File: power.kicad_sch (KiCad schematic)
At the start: 116 parts, among them J3 Conn_01x01, J4 Conn_01x01, U16 CSD95472Q5MC, U3 TPS53647, U36 MCP1824T-1802E, U4 CSD95472Q5MC, U5 CSD95472Q5MC, U6 AP3211, U7 MCP1824T-0802E

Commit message: Added 4th Phase Buck
Started to add 4th Phase for the Buck, implementing BM1370 footprint etc
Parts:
- added C198: 100n/0.7mm, Capacitor_SMD:C_0805_2012Metric, symbol Device:C
- added C199: 2.2µ, Capacitor_SMD:C_0805_2012Metric, symbol Device:C
- added C200: 100n, Capacitor_SMD:C_0805_2012Metric, symbol Device:C
- added C201, C202: 1n/0.7mm, Capacitor_SMD:C_0805_2012Metric, symbol Device:C
- added C206, C207: 100µ/6.3V, Capacitor_SMD:C_1210_3225Metric, symbol Device:C
- added C208, C209, C210, C214: 330µ/4V, Capacitor_SMD:C_1210_3225Metric, symbol Device:C
- added C215: 3.3n/25V, Capacitor_SMD:C_0805_2012Metric, symbol Device:C
- added C216: 1µ/25V, Capacitor_SMD:C_0805_2012Metric, symbol Device:C
- added C217: 10µ, Capacitor_SMD:C_0805_2012Metric, symbol Device:C
- added C218: 220µ/25V, Capacitor_SMD:CP_Elec_8x10, symbol Device:C_Polarized
- added C222, C223, C224: 22µ/25V, Capacitor_SMD:C_1210_3225Metric, symbol Device:C
- added L5: 220nH, Qaxe:IFLR-4031GC-01-8x10, symbol Device:L
- added R52, R53: 1R/0.5W, Resistor_SMD:R_0805_2012Metric, symbol Device:R
- added U1: CSD95472Q5MC, myfootprints:CSD95472-SON-5x6, symbol mylib7:CSD95472Q5MC
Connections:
- net +12V: now also C215.1, C216.1, C218.1, C222.1, C223.1, C224.1, U1.7 (VIN)
- net +1V2: now also C206.1, C207.1, C208.1, C209.1, C210.1, C214.1, L5.2
- net +3V3: no longer U3.6 (CSP4)
- net +5V: now also C217.1, R52.1
- net +VRef: now also C198.1, U1.2 (REFIN)
- net FCCM: now also U1.10 (FCCM)
- net GND: now also C198.2, C199.2, C201.2, C202.2, C206.2, C207.2, C208.2, C209.2, C210.2, C214.2, C215.2, C216.2, C217.2, C218.2, C222.2, C223.2, C224.2, U1.13 (PGND), U1.4 (PGND)
- net TPS_TSEN: now also C202.1, U1.11 (TAO/FAULT)
- net TPS_PWM4: now reaches U3.35 (PWM4)
- net TPS_PWM4: now also U1.12 (PWM)
- new net: C201.1, R53.1
- new net: L5.1, R53.2, U1.6 (VSW)
- new net: C199.1, R52.2, U1.3 (ENABLE), U1.5 (VDD)
- new net: C200.2, U1.8 (BOOT_R)
- new net: C200.1, U1.9 (BOOT)
- new net TPS_CSP4: U1.1 (IOUT), U3.6 (CSP4)
- no-connect marks 11 -> 10
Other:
- moved on the sheet: C1, C10, C100, C104, C106, C109, C11, C110, C112, C113, C117, C118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

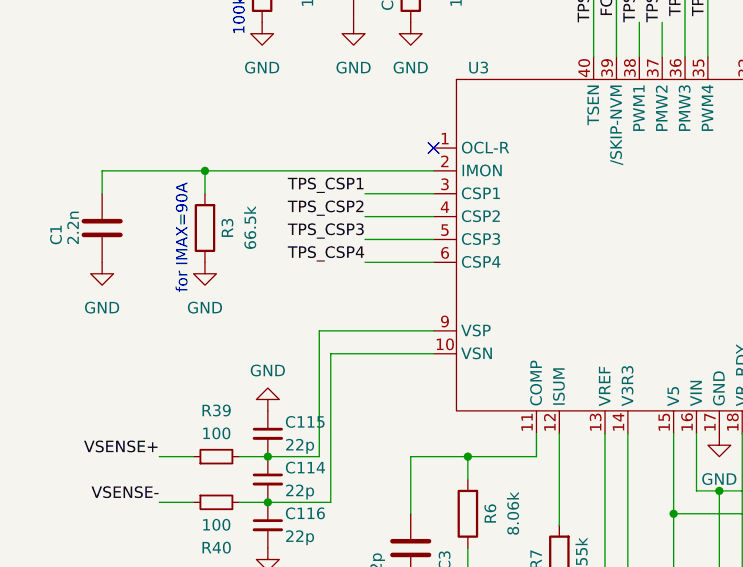
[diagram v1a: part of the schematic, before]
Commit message: Phase4 Disable
Phase4-Disable Jumper
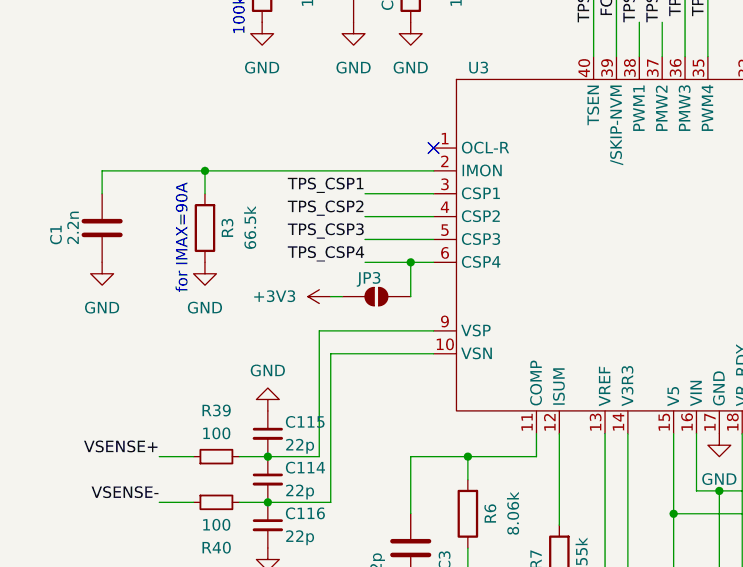
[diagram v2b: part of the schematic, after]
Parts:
- added JP3: Disable Phase 4, Jumper:SolderJumper-2_P1.3mm_Open_RoundedPad1.0x1.5mm, symbol Jumper:SolderJumper_2_Open
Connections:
- net +3V3: now also JP3.1 (A)
- net TPS_CSP4: now also JP3.2 (B)
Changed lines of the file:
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@@
 	)
 	(junction
+		(at 62.23 123.19)
+		(diameter 0)
+		(color 0 0 0 0)
+	)
+	(junction
 		(at 354.33 120.65)
 		(diameter 0)
@@
 	(wire
 		(pts
+			(xy 53.34 127) (xy 54.61 127)
+		)
+		(stroke
+			(width 0)
+			(type default)
+		)
+	)
+	(wire
+		(pts
 			(xy 190.5 50.8) (xy 195.58 50.8)
 		)
@@
 	(wire
 		(pts
-			(xy 57.15 123.19) (xy 64.77 123.19)
+			(xy 57.15 123.19) (xy 62.23 123.19)
 		)
 		(stroke
@@
 	(wire
 		(pts
+			(xy 62.23 127) (xy 62.23 123.19)
+		)
+		(stroke
+			(width 0)
+			(type default)
+		)
+	)
+	(wire
+		(pts
 			(xy 43.18 149.86) (xy 46.355 149.86)
 		)
@@
 	(wire
 		(pts
+			(xy 62.23 123.19) (xy 64.77 123.19)
+		)
+		(stroke
+			(width 0)
+			(type default)
+		)
+	)
+	(wire
+		(pts
 			(xy 311.15 116.84) (xy 311.15 120.65)
 		)
@@
 	)
 	(symbol
+		(lib_id "Jumper:SolderJumper_2_Open")
+		(at 58.42 127 0)
+		(unit 1)
+		(exclude_from_sim yes)
+		(in_bom no)
+		(on_board yes)
+		(dnp no)
+		(property "Reference" "JP3"
+			(at 57.658 124.968 0)
+			(effects
+				(font
+					(size 1.27 1.27)
+				)
+			)
+		)
+		(property "Value" "Disable Phase 4"
+			(at 55.372 129.032 0)
+			(effects
+				(font
+					(size 1.27 1.27)
+				)
+				(hide yes)
+			)
+		)
+		(property "Footprint" "Jumper:SolderJumper-2_P1.3mm_Open_RoundedPad1.0x1.5mm"
+			(at 58.42 127 0)
+			(effects
+				(font
+					(size 1.27 1.27)
+				)
+				(hide yes)
+			)
+		)
+		(property "Datasheet" "~"
+			(at 58.42 127 0)
+			(effects
+				(font
+					(size 1.27 1.27)
+				)
+				(hide yes)
+			)
+		)
+		(property "Description" "Solder Jumper, 2-pole, open"
+			(at 58.42 127 0)
+			(effects
+				(font
+					(size 1.27 1.27)
+				)
+				(hide yes)
+			)
+		)
+		(pin "2"
+		)
+		(pin "1"
+		)
+		(instances
+			(project "Nerd8"
+				(path "/e63e39d7-6ac0-4ffd-8aa3-1841a4541b55/8ec0a9c6-2b78-44ef-a83d-9047d2828409"
+					(reference "JP3")
+					(unit 1)
+				)
+			)
+		)
+	)
+	(symbol
 		(lib_id "Device:C")
 		(at 195.58 68.58 0)
@@
 					(unit 1)
 				)
+			)
+		)
+	)
+	(symbol
+		(lib_name "+3V3_2")
+		(lib_id "power:+3V3")
+		(at 53.34 127 90)
+		(unit 1)
+		(exclude_from_sim no)
+		(in_bom yes)
+		(on_board yes)
+		(dnp no)
+		(fields_autoplaced yes)
+		(property "Reference" "#PWR0363"
+			(at 57.15 127 0)
+			(effects
+				(font
+					(size 1.27 1.27)
+				)
+				(hide yes)
+			)
+		)
+		(property "Value" "+3V3"
+			(at 49.53 126.9999 90)
+			(effects
+				(font
+					(size 1.27 1.27)
+				)
+				(justify left)
+			)
+		)
+		(property "Footprint" ""
+			(at 53.34 127 0)
+			(effects
+				(font
+					(size 1.27 1.27)
+				)
+				(hide yes)
+			)
+		)
+		(property "Datasheet" ""
+			(at 53.34 127 0)
+			(effects
+				(font
+					(size 1.27 1.27)
+				)
+				(hide yes)
+			)
+		)
+		(property "Description" "Power symbol creates a global label with name \"+3V3\""
+			(at 53.34 127 0)
+			(effects
+				(font
+					(size 1.27 1.27)
+				)
+				(hide yes)
+			)
+		)
+		(pin "1"
+		)
+		(instances
+			(project "Nerd8"
+				(path "/e63e39d7-6ac0-4ffd-8aa3-1841a4541b55/8ec0a9c6-2b78-44ef-a83d-9047d2828409"
+					(reference "#PWR0363")
+					(unit 1)
+				)

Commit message: Changed LDO to 1V2 and original 1V2 to VDD
1V8 LDO replaced with 1V2 LDO
Crystal replaced
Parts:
- U36: value MCP1824T-1802E -> MCP1824T-1202E; Manufacturer MCP1824T-1802E/OT -> MCP1824T-1202E/OT; OrderNr MCP1824T-1802E/OTCT-ND -> MCP1824T-1202E/OTCT-ND
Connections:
- net +1V8 is gone; now on net +1V2: C108.1, U36.5 (VOUT)
- net +1V2: no longer C184.1, C185.1, C186.1, C187.1, C188.1, C189.1, C194.1, C206.1, C207.1, C208.1, C209.1, C21.1, C210.1, C214.1, C22.1, C24.1, C39.1, C48.1, C84.1, C86.1, C90.1, C91.1, C95.1, C97.1, C98.1, C99.1, J3.1 (Pin_1), L1.2, L2.2, L4.2, L5.2, R29.2
- new net VDD: C184.1, C185.1, C186.1, C187.1, C188.1, C189.1, C194.1, C206.1, C207.1, C208.1, C209.1, C21.1, C210.1, C214.1, C22.1, C24.1, C39.1, C48.1, C84.1, C86.1, C90.1, C91.1, C95.1, C97.1, C98.1, C99.1, J3.1 (Pin_1), L1.2, L2.2, L4.2, L5.2, R29.2
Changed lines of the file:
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@@
 		)
 	)
-	(hierarchical_label "+1V2"
+	(hierarchical_label "VDD"
 		(shape output)
 		(at 31.75 26.67 180)
@@
 		)
 	)
-	(hierarchical_label "+1V8"
+	(hierarchical_label "+1V2"
 		(shape output)
 		(at 31.75 34.29 180)
@@
 	)
 	(symbol
-		(lib_id "power:+1V2")
+		(lib_id "power:VDD")
 		(at 429.26 101.6 0)
 		(unit 1)
@@
 			)
 		)
-		(property "Value" "+1V2"
-			(at 429.26 96.52 0)
+		(property "Value" "VDD"
+			(at 431.8 100.3299 0)
 			(effects
 				(font
 					(size 1.27 1.27)
 				)
+				(justify left)
 			)
 		)
@@
 			)
 		)
-		(property "Description" ""
+		(property "Description" "Power symbol creates a global label with name \"VDD\""
 			(at 429.26 101.6 0)
 			(effects
@@
 	)
 	(symbol
-		(lib_id "power:+1V8")
+		(lib_id "power:+1V2")
 		(at 39.37 34.29 270)
 		(mirror x)
@@
 			)
 		)
-		(property "Value" "+1V8"
-			(at 43.18 34.29 90)
+		(property "Value" "+1V2"
+			(at 43.18 34.2899 90)
 			(effects
 				(font
@@
 			)
 		)
-		(property "Description" ""
+		(property "Description" "Power symbol creates a global label with name \"+1V2\""
 			(at 39.37 34.29 0)
 			(effects
@@
 			)
 		)
-		(property "Value" "MCP1824T-1802E"
+		(property "Value" "MCP1824T-1202E"
 			(at 215.265 253.365 0)
 			(effects
@@
 			)
 		)
-		(property "OrderNr" "MCP1824T-1802E/OTCT-ND"
+		(property "OrderNr" "MCP1824T-1202E/OTCT-ND"
 			(at 215.265 258.445 0)
 			(effects
@@
 			)
 		)
-		(property "Manufacturer" "MCP1824T-1802E/OT"
+		(property "Manufacturer" "MCP1824T-1202E/OT"
 			(at 215.265 258.445 0)
 			(effects
@@
 	)
 	(symbol
-		(lib_id "power:+1V8")
+		(lib_id "power:+1V2")
 		(at 233.045 255.905 0)
 		(unit 1)
@@
 			)
 		)
-		(property "Value" "+1V8"
-			(at 233.045 251.46 0)
+		(property "Value" "+1V2"
+			(at 234.95 254.6349 0)
 			(effects
 				(font
 					(size 1.27 1.27)
 				)
+				(justify left)
 			)
 		)
@@
 			)
 		)
-		(property "Description" ""
+		(property "Description" "Power symbol creates a global label with name \"+1V2\""
 			(at 233.045 255.905 0)
 			(effects
@@
 	)
 	(symbol
-		(lib_id "power:+1V2")
+		(lib_id "power:VDD")
 		(at 39.37 26.67 270)
 		(mirror x)
@@
 			)
 		)
-		(property "Value" "+1V2"
-			(at 42.545 26.67 90)
+		(property "Value" "VDD"
+			(at 43.18 26.6699 90)
 			(effects
 				(font
@@
 			)
 		)
-		(property "Description" ""
+		(property "Description" "Power symbol creates a global label with name \"VDD\""
 			(at 39.37 26.67 0)
 			(effects

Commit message: minor chages
R3 to 49.9K
added DK-Bom
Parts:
- C112, C117, C181, C215: Distributor (none) -> D; OrderNr (none) -> 490-8291-1-ND
- C3: Distributor (none) -> D; OrderNr (none) -> 478-KGM15ACG2A120JMCT-ND
- R1: Distributor (none) -> D; OrderNr (none) -> 541-16.5KCCT-ND
- R2: Distributor (none) -> D; OrderNr (none) -> 311-24.3KCRCT-ND
- R3: value 66.5k -> 49.9k; Distributor (none) -> D; OrderNr (none) -> 311-49.9KCRCT-ND
- R34: Distributor (none) -> D; OrderNr (none) -> RMCF0805FT16K2CT-ND
- R5: Distributor (none) -> D; OrderNr (none) -> RMCF0805FT121KCT-ND
- R7: Distributor (none) -> D; OrderNr (none) -> 311-2.55KCRCT-ND
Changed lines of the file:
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@@
 			)
 		)
-		(property "Distributor" ""
+		(property "Distributor" "D"
 			(at 62.23 154.94 0)
 			(effects
@@
 			)
 		)
-		(property "OrderNr" ""
+		(property "OrderNr" "478-KGM15ACG2A120JMCT-ND"
 			(at 62.23 154.94 0)
 			(effects
@@
 			)
 		)
-		(property "Distributor" ""
+		(property "Distributor" "D"
 			(at 265.43 26.67 0)
 			(effects
@@
 			)
 		)
-		(property "OrderNr" ""
+		(property "OrderNr" "490-8291-1-ND"
 			(at 265.43 26.67 0)
 			(effects
@@
 			)
 		)
+		(property "Distributor" "D"
+			(at 125.73 97.155 90)
+			(effects
+				(font
+					(size 1.27 1.27)
+				)
+				(hide yes)
+			)
+		)
+		(property "OrderNr" "541-16.5KCCT-ND"
+			(at 125.73 97.155 90)
+			(effects
+				(font
+					(size 1.27 1.27)
+				)
+				(hide yes)
+			)
+		)
 		(pin "1"
 		)
@@
 			)
 		)
-		(property "Distributor" ""
+		(property "Distributor" "D"
 			(at 285.75 26.67 0)
 			(effects
@@
 			)
 		)
-		(property "OrderNr" ""
+		(property "OrderNr" "490-8291-1-ND"
 			(at 285.75 26.67 0)
 			(effects
@@
 			)
 		)
-		(property "Distributor" ""
+		(property "Distributor" "D"
 			(at 305.435 26.67 0)
 			(effects
@@
 			)
 		)
-		(property "OrderNr" ""
+		(property "OrderNr" "490-8291-1-ND"
 			(at 305.435 26.67 0)
 			(effects
@@
 			)
 		)
-		(property "Distributor" ""
+		(property "Distributor" "D"
 			(at 72.39 233.68 0)
 			(effects
@@
 			)
 		)
-		(property "OrderNr" ""
+		(property "OrderNr" "RMCF0805FT16K2CT-ND"
 			(at 72.39 233.68 0)
 			(effects
@@
 			)
 		)
+		(property "Distributor" "D"
+			(at 125.73 106.045 90)
+			(effects
+				(font
+					(size 1.27 1.27)
+				)
+				(hide yes)
+			)
+		)
+		(property "OrderNr" "311-24.3KCRCT-ND"
+			(at 125.73 106.045 90)
+			(effects
+				(font
+					(size 1.27 1.27)
+				)
+				(hide yes)
+			)
+		)
 		(pin "1"
 		)
@@
 			)
 		)
-		(property "Value" "66.5k"
+		(property "Value" "49.9k"
 			(at 44.45 119.38 90)
 			(effects
@@
 			)
 		)
+		(property "Distributor" "D"
+			(at 39.37 119.38 90)
+			(effects
+				(font
+					(size 1.27 1.27)
+				)
+				(hide yes)
+			)
+		)
+		(property "OrderNr" "311-49.9KCRCT-ND"
+			(at 39.37 119.38 90)
+			(effects
+				(font
+					(size 1.27 1.27)
+				)
+				(hide yes)
+			)
+		)
 		(pin "1"
 		)
@@
 			)
 		)
-		(property "Distributor" ""
+		(property "Distributor" "D"
 			(at 325.755 25.4 0)
 			(effects
@@
 			)
 		)
-		(property "OrderNr" ""
+		(property "OrderNr" "490-8291-1-ND"
 			(at 325.755 25.4 0)
 			(effects
@@
 			)
 		)
+		(property "Distributor" "D"
+			(at 78.74 156.21 90)
+			(effects
+				(font
+					(size 1.27 1.27)
+				)
+				(hide yes)
+			)
+		)
+		(property "OrderNr" "311-2.55KCRCT-ND"
+			(at 78.74 156.21 90)
+			(effects
+				(font
+					(size 1.27 1.27)
+				)
+				(hide yes)
+			)
+		)
 		(pin "1"
 		)
@@
 			(effects
 				(font
+					(size 1.27 1.27)
+				)
+				(hide yes)
+			)
+		)
+		(property "Distributor" "D"
+			(at 62.23 92.71 90)
+			(effects
+				(font
+					(size 1.27 1.27)
+				)
+				(hide yes)
+			)
+		)
+		(property "OrderNr" "RMCF0805FT121KCT-ND"
+			(at 62.23 92.71 90)
+			(effects
+				(font

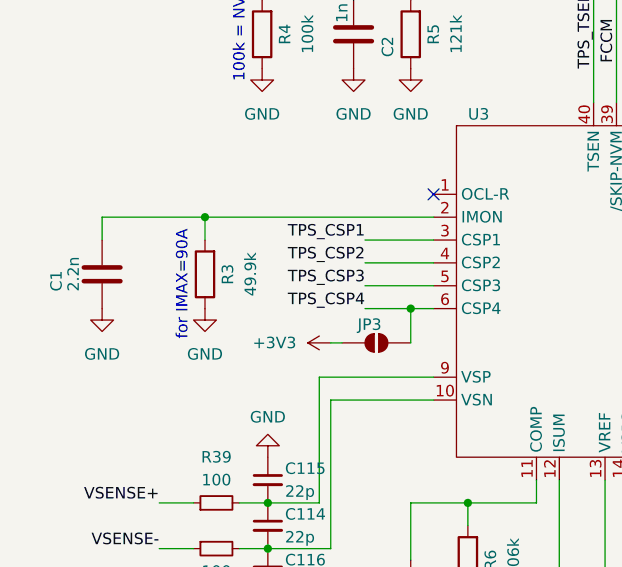
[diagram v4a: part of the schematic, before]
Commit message: changed imon to 33,2k for 180Amps
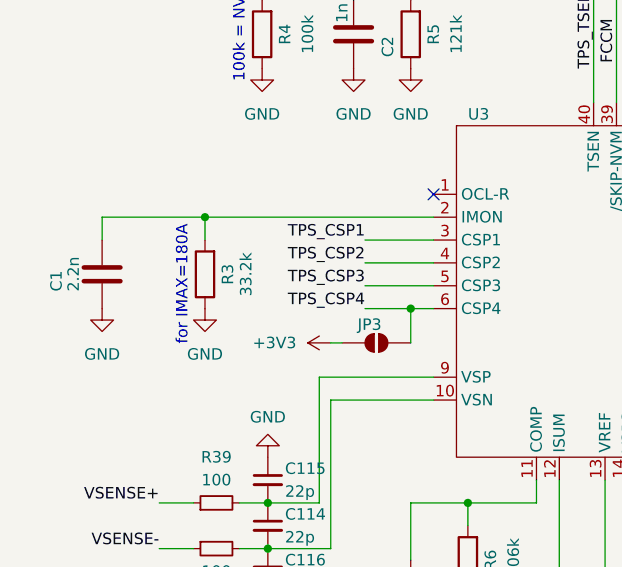
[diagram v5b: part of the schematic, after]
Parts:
- R3: value 49.9k -> 33.2k; OrderNr 311-49.9KCRCT-ND -> RMCF0805FT33K2CT-ND
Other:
- note added: "for IMAX=180A"
- note removed: "for IMAX=90A"
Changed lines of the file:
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@@
 		)
 	)
-	(text "for IMAX=90A"
+	(text "for IMAX=180A"
 		(exclude_from_sim no)
 		(at 36.83 120.65 90)
@@
 			)
 		)
-		(property "Value" "49.9k"
-			(at 44.45 119.38 90)
+		(property "Value" "33.2k"
+			(at 43.942 119.38 90)
 			(effects
 				(font
@@
 			)
 		)
-		(property "OrderNr" "311-49.9KCRCT-ND"
+		(property "OrderNr" "RMCF0805FT33K2CT-ND"
 			(at 39.37 119.38 90)
 			(effects
